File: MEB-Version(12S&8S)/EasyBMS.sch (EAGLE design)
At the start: 168 parts, among them IC1 XL7046, IC2 LTC6811IG-1#PBF, IC3 ISO1042DWV, IC4 C98655, J1 TYPE-C-31-M-12, Q14 C8547, Q15 C8547, Q16 C8547, Q18 C8547, Q20 C8547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

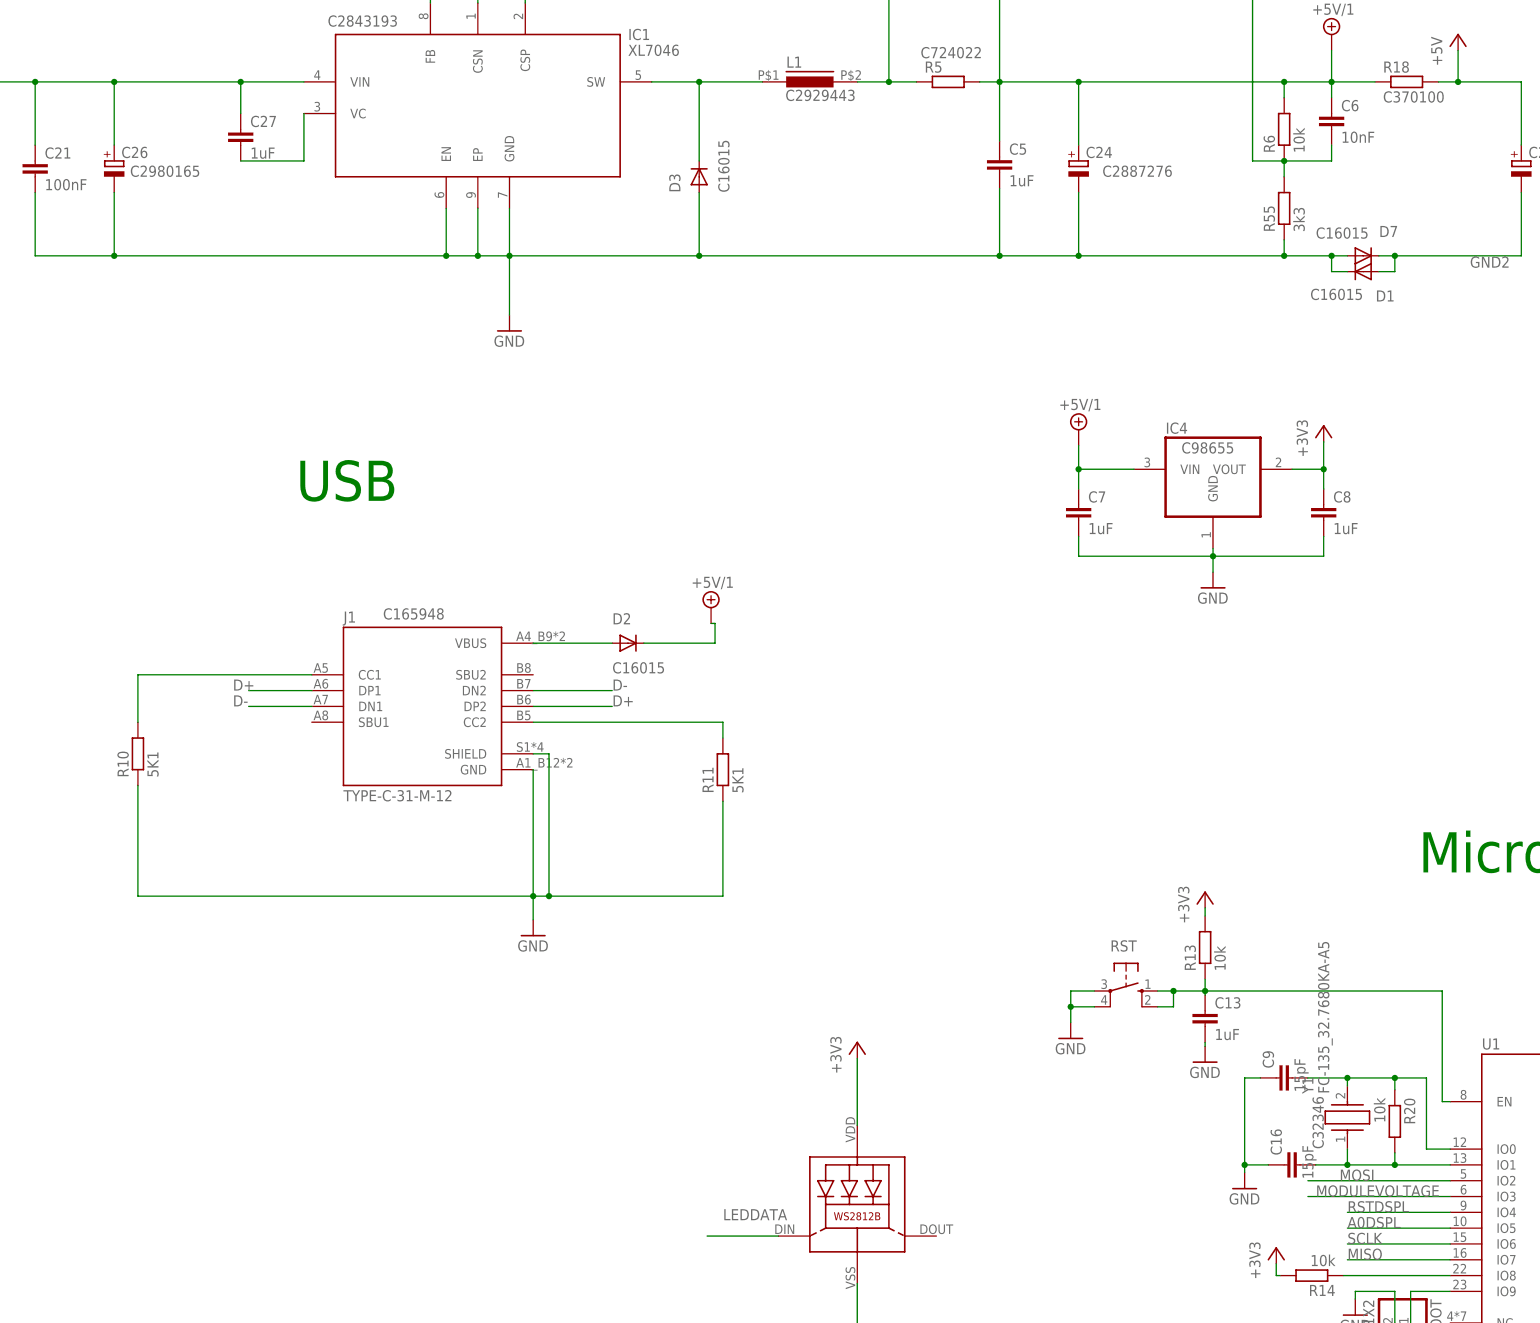
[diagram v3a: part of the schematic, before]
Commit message: change some parts to basic parts, add USB protection
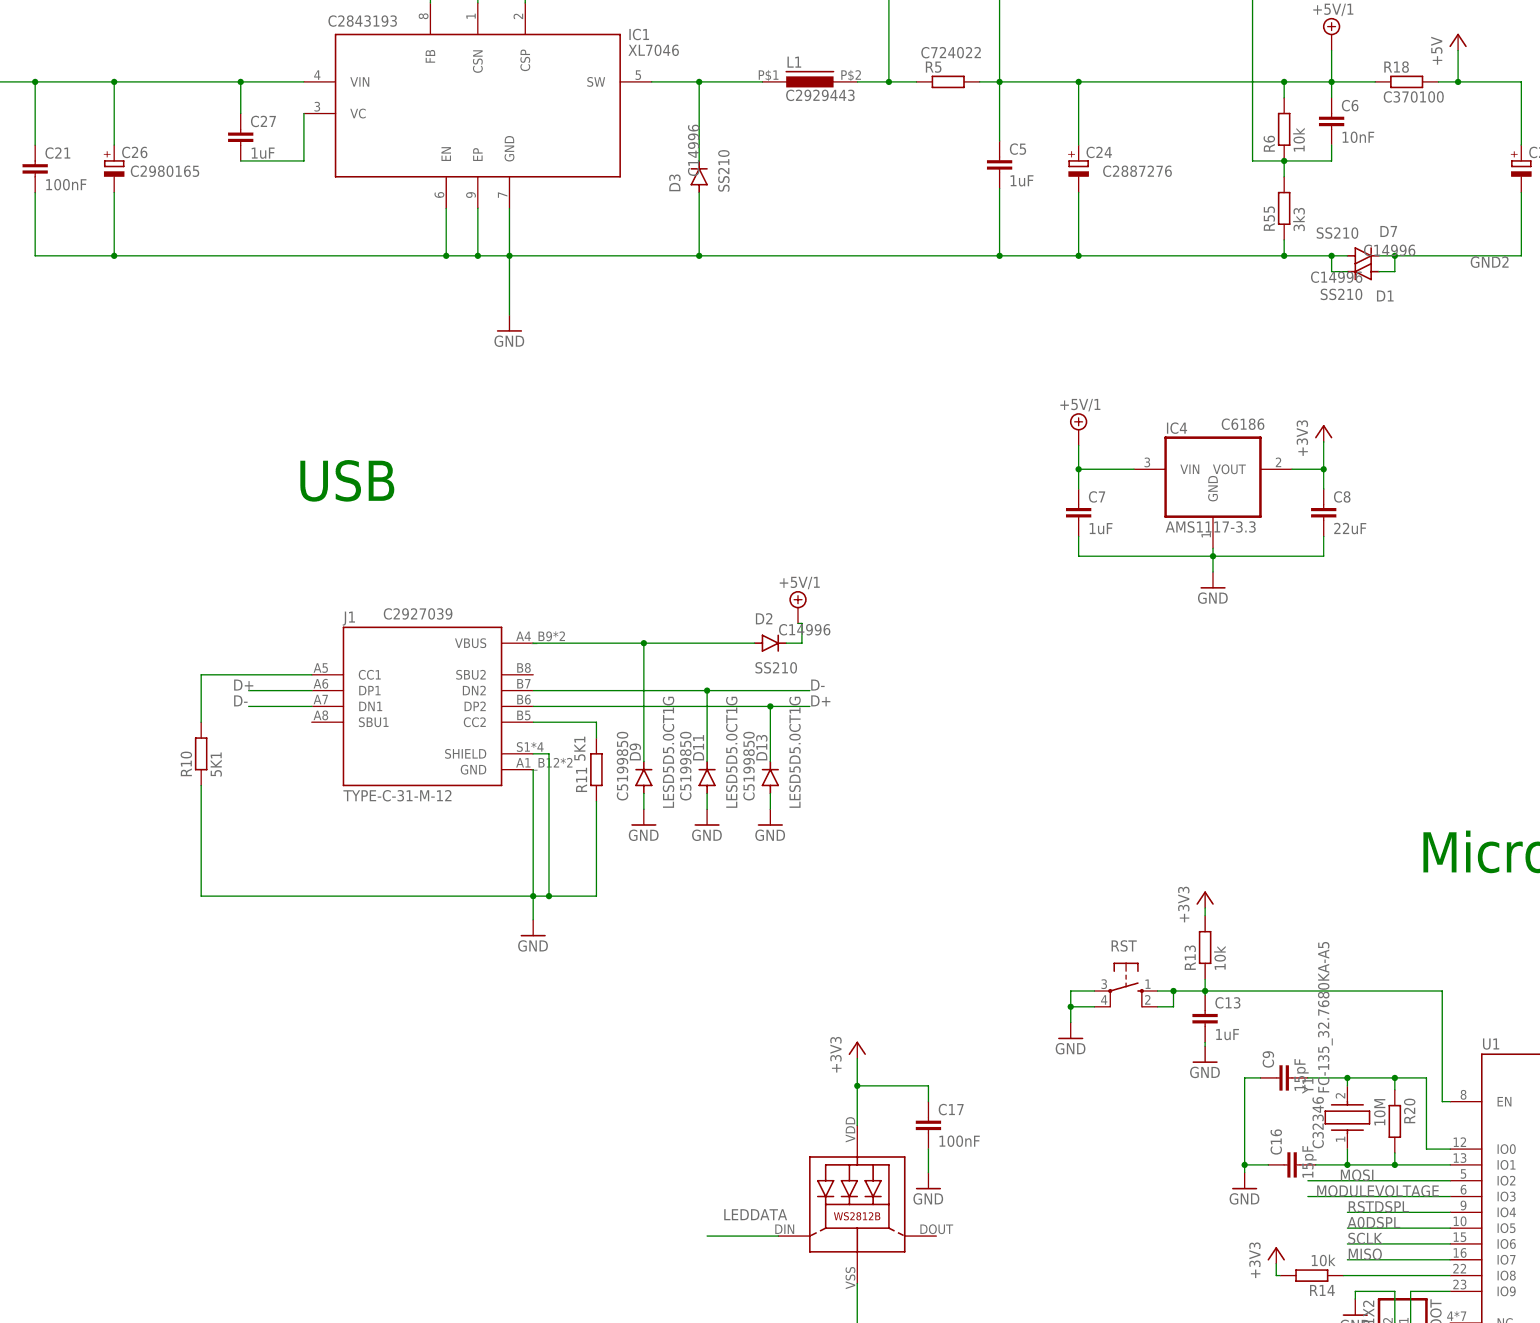
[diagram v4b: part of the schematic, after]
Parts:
- added C17: 100nF, rcl:C-EUC0402
- added D11, D13, D9: LESD5D5.0CT1G, diode:DIODE-SOD523
- C14: device rcl:C-EUC1206 -> rcl:C-EUC0805
- C8: value 1uF -> 22uF; device rcl:C-EUC0402 -> rcl:C-EUC0603
- D1, D2, D3, D7: value C16015 -> SS210; LCSC (none) -> C14996
- IC4: value C98655 -> AMS1117-3.3; LCSC (none) -> C6186
- J1: LCSC C165948 -> C2927039
- R20: value 10k -> 10M
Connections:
- net +3V3: now also C17.1
- net D+: now also D13.C
- net D-: now also D11.C
- net GND: now also C17.2, D11.A, D13.A, D9.A
- net N$4: now also D9.C
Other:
- moved on the sheet: R10, R11

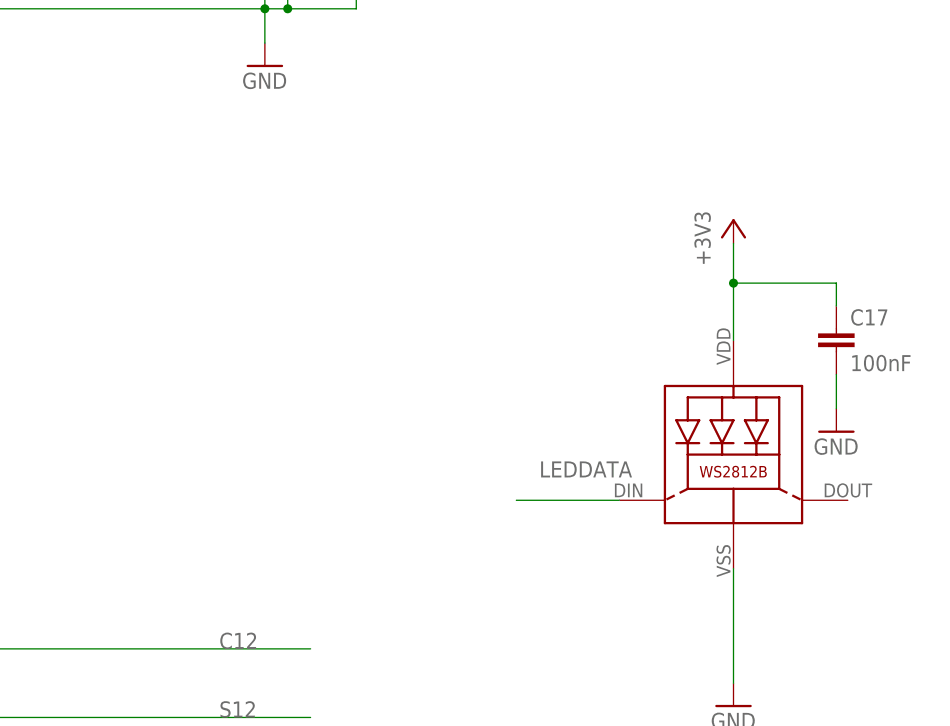
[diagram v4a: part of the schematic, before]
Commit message: change LED pixel circuit as in C6 Devkit
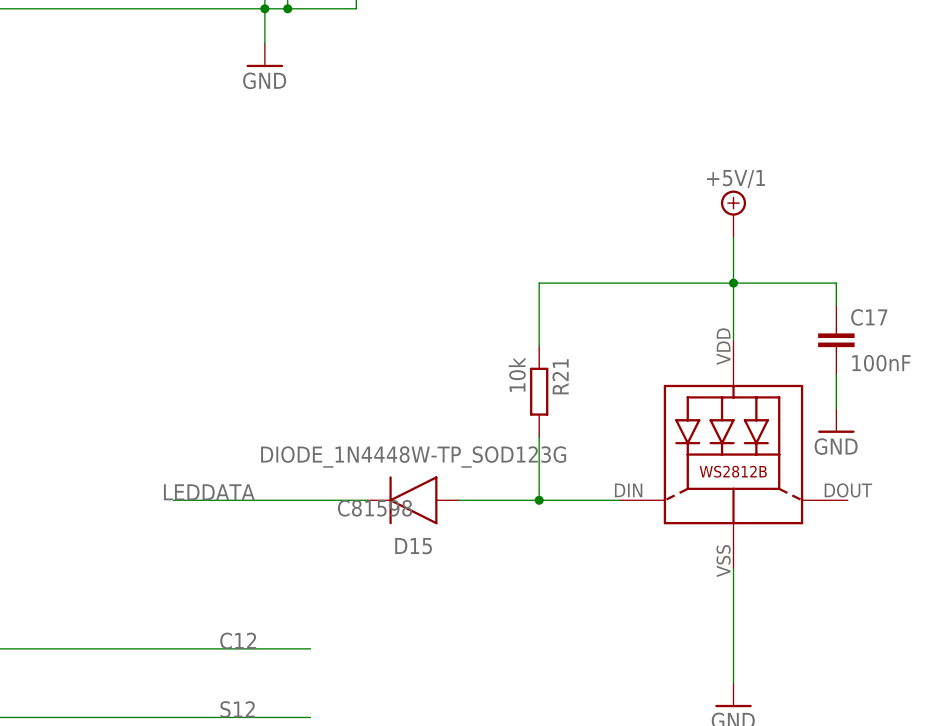
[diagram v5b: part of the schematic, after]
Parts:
- added D15: DIODE_1N4448W-TP_SOD123G, Diode:DIODE_1N4448W-TP_SOD123G
- added R21: 10k, rcl:R-EU_R0402
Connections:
- new net N$24: D15.A, LED2.DI, R21.2
- net +3V3: no longer C17.1, LED2.VDD
- net +5V/1: now also C17.1, LED2.VDD, R21.1
- net LEDDATA: now also D15.C; no longer LED2.DI
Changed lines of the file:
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@@
 <part name="TERM" library="jumper" library_urn="urn:adsk.eagle:library:252" deviceset="SJ" device="" package3d_urn="urn:adsk.eagle:package:15471/1"/>
 <part name="C12" library="rcl" library_urn="urn:adsk.eagle:library:334" deviceset="C-EU" device="C1206" package3d_urn="urn:adsk.eagle:package:23618/2" value="47µF"/>
-<part name="+3V7" library="supply1" library_urn="urn:adsk.eagle:library:371" deviceset="+3V3" device=""/>
 <part name="R13" library="rcl" library_urn="urn:adsk.eagle:library:334" deviceset="R-EU_" device="R0402" package3d_urn="urn:adsk.eagle:package:23547/3" value="10k"/>
 <part name="C13" library="rcl" library_urn="urn:adsk.eagle:library:334" deviceset="C-EU" device="C0402" package3d_urn="urn:adsk.eagle:package:23626/2" value="1uF"/>
@@
 <part name="GND18" library="supply1" library_urn="urn:adsk.eagle:library:371" deviceset="GND" device=""/>
 <part name="GND19" library="supply1" library_urn="urn:adsk.eagle:library:371" deviceset="GND" device=""/>
+<part name="SUPPLY3" library="supply2" library_urn="urn:adsk.eagle:library:372" deviceset="+5V/1" device=""/>
+<part name="D15" library="Diode" library_urn="urn:adsk.eagle:library:16378169" deviceset="DIODE_" device="_SOD123G" package3d_urn="urn:adsk.eagle:package:9427058/2" technology="1N4448W-TP">
+<attribute name="LCSC" value="C81598"/>
+</part>
+<part name="R21" library="rcl" library_urn="urn:adsk.eagle:library:334" deviceset="R-EU_" device="R0402" package3d_urn="urn:adsk.eagle:package:23547/3" value="10k"/>
 </parts>
 <sheets>
@@
 <attribute name="VALUE" x="-9.906" y="446.151" size="1.778" layer="96"/>
 </instance>
-<instance part="+3V7" gate="G$1" x="-220.98" y="511.175" smashed="yes">
-<attribute name="VALUE" x="-223.52" y="506.095" size="1.778" layer="96" rot="R90"/>
-</instance>
 <instance part="R13" gate="G$1" x="-165.1" y="526.415" smashed="yes" rot="R90">
 <attribute name="NAME" x="-166.5986" y="522.605" size="1.778" layer="95" rot="R90"/>
@@
 <attribute name="VALUE" x="-237.49" y="543.56" size="1.778" layer="96"/>
 </instance>
+<instance part="SUPPLY3" gate="G$1" x="-220.98" y="511.81" smashed="yes">
+<attribute name="VALUE" x="-224.155" y="514.985" size="1.778" layer="96"/>
+</instance>
+<instance part="D15" gate="G$1" x="-256.54" y="480.06" smashed="yes" rot="R180">
+<attribute name="NAME" x="-256.54" y="474.98" size="1.778" layer="95" rot="R180" align="center"/>
+<attribute name="VALUE" x="-256.54" y="485.14" size="1.778" layer="96" rot="R180" align="center"/>
+<attribute name="LCSC" x="-256.54" y="480.06" size="1.778" layer="96" rot="R180"/>
+</instance>
+<instance part="R21" gate="G$1" x="-242.57" y="492.125" smashed="yes" rot="R270">
+<attribute name="NAME" x="-241.0714" y="495.935" size="1.778" layer="95" rot="R270"/>
+<attribute name="VALUE" x="-245.872" y="495.935" size="1.778" layer="96" rot="R270"/>
+</instance>
 </instances>
 <busses>
@@
 </segment>
 <segment>
-<pinref part="LED2" gate="G$1" pin="VDD"/>
-<wire x1="-220.98" y1="497.84" x2="-220.98" y2="504.19" width="0.1524" layer="91"/>
-<pinref part="+3V7" gate="G$1" pin="+3V3"/>
-<pinref part="C17" gate="G$1" pin="1"/>
-<wire x1="-220.98" y1="504.19" x2="-220.98" y2="508.635" width="0.1524" layer="91"/>
-<wire x1="-220.98" y1="504.19" x2="-209.55" y2="504.19" width="0.1524" layer="91"/>
-<wire x1="-209.55" y1="504.19" x2="-209.55" y2="501.65" width="0.1524" layer="91"/>
-<junction x="-220.98" y="504.19"/>
-</segment>
-<segment>
 <pinref part="+3V5" gate="G$1" pin="+3V3"/>
 <pinref part="R13" gate="G$1" pin="2"/>
@@
 <wire x1="-53.34" y1="480.06" x2="-53.34" y2="490.22" width="0.1524" layer="91"/>
 </segment>
+<segment>
+<pinref part="LED2" gate="G$1" pin="VDD"/>
+<wire x1="-220.98" y1="497.84" x2="-220.98" y2="504.19" width="0.1524" layer="91"/>
+<pinref part="C17" gate="G$1" pin="1"/>
+<wire x1="-220.98" y1="504.19" x2="-220.98" y2="509.27" width="0.1524" layer="91"/>
+<wire x1="-220.98" y1="504.19" x2="-209.55" y2="504.19" width="0.1524" layer="91"/>
+<wire x1="-209.55" y1="504.19" x2="-209.55" y2="501.65" width="0.1524" layer="91"/>
+<junction x="-220.98" y="504.19"/>
+<pinref part="SUPPLY3" gate="G$1" pin="+5V/1"/>
+<pinref part="R21" gate="G$1" pin="1"/>
+<wire x1="-242.57" y1="497.205" x2="-242.57" y2="504.19" width="0.1524" layer="91"/>
+<wire x1="-242.57" y1="504.19" x2="-220.98" y2="504.19" width="0.1524" layer="91"/>
+</segment>
 </net>
 <net name="C12+POWER" class="0">
@@
 <net name="LEDDATA" class="0">
 <segment>
-<pinref part="LED2" gate="G$1" pin="DI"/>
-<wire x1="-233.68" y1="480.06" x2="-245.11" y2="480.06" width="0.1524" layer="91"/>
-<label x="-242.57" y="482.6" size="1.778" layer="95"/>
-</segment>
-<segment>
 <pinref part="U1" gate="G$1" pin="IO14"/>
 <wire x1="-95.25" y1="488.95" x2="-85.09" y2="488.95" width="0.1524" layer="91"/>
 <label x="-95.25" y="488.95" size="1.778" layer="95"/>
 </segment>
+<segment>
+<pinref part="D15" gate="G$1" pin="C"/>
+<wire x1="-261.62" y1="480.06" x2="-283.21" y2="480.06" width="0.1524" layer="91"/>
+<label x="-284.48" y="480.06" size="1.778" layer="95"/>
+</segment>
 </net>
 <net name="SCLK" class="0">
@@
 </segment>
 </net>
+<net name="N$24" class="0">
+<segment>
+<pinref part="LED2" gate="G$1" pin="DI"/>
+<pinref part="D15" gate="G$1" pin="A"/>
+<wire x1="-233.68" y1="480.06" x2="-242.57" y2="480.06" width="0.1524" layer="91"/>
+<pinref part="R21" gate="G$1" pin="2"/>
+<wire x1="-242.57" y1="480.06" x2="-251.46" y2="480.06" width="0.1524" layer="91"/>
+<wire x1="-242.57" y1="487.045" x2="-242.57" y2="480.06" width="0.1524" layer="91"/>
+<junction x="-242.57" y="480.06"/>
+</segment>
+</net>

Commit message: new Footprint to change to basic parts
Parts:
- C12, C14: value 47µF -> 47uF
- R15, R16: device rcl:R-EU_R0402 -> rcl:R-EU_R0603
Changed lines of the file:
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@@
 </classes>
 <parts>
-<part name="R15" library="rcl" library_urn="urn:adsk.eagle:library:334" deviceset="R-EU_" device="R0402" package3d_urn="urn:adsk.eagle:package:23547/3" value="470k"/>
-<part name="R16" library="rcl" library_urn="urn:adsk.eagle:library:334" deviceset="R-EU_" device="R0402" package3d_urn="urn:adsk.eagle:package:23547/3" value="27K"/>
+<part name="R15" library="rcl" library_urn="urn:adsk.eagle:library:334" deviceset="R-EU_" device="R0603" package3d_urn="urn:adsk.eagle:package:23555/3" value="470k"/>
+<part name="R16" library="rcl" library_urn="urn:adsk.eagle:library:334" deviceset="R-EU_" device="R0603" package3d_urn="urn:adsk.eagle:package:23555/3" value="27K"/>
 <part name="C4" library="rcl" library_urn="urn:adsk.eagle:library:334" deviceset="C-EU" device="C0402" package3d_urn="urn:adsk.eagle:package:23626/2" value="1uF"/>
 <part name="C19" library="rcl" library_urn="urn:adsk.eagle:library:334" deviceset="C-EU" device="C0402" package3d_urn="urn:adsk.eagle:package:23626/2" value="1uF"/>
@@
 <part name="R12" library="rcl" library_urn="urn:adsk.eagle:library:334" deviceset="R-EU_" device="R0402" package3d_urn="urn:adsk.eagle:package:23547/3" value="120R"/>
 <part name="TERM" library="jumper" library_urn="urn:adsk.eagle:library:252" deviceset="SJ" device="" package3d_urn="urn:adsk.eagle:package:15471/1"/>
-<part name="C12" library="rcl" library_urn="urn:adsk.eagle:library:334" deviceset="C-EU" device="C1206" package3d_urn="urn:adsk.eagle:package:23618/2" value="47µF"/>
+<part name="C12" library="rcl" library_urn="urn:adsk.eagle:library:334" deviceset="C-EU" device="C1206" package3d_urn="urn:adsk.eagle:package:23618/2" value="47uF"/>
 <part name="R13" library="rcl" library_urn="urn:adsk.eagle:library:334" deviceset="R-EU_" device="R0402" package3d_urn="urn:adsk.eagle:package:23547/3" value="10k"/>
 <part name="C13" library="rcl" library_urn="urn:adsk.eagle:library:334" deviceset="C-EU" device="C0402" package3d_urn="urn:adsk.eagle:package:23626/2" value="1uF"/>
 <part name="GND11" library="supply1" library_urn="urn:adsk.eagle:library:371" deviceset="GND" device=""/>
-<part name="C14" library="rcl" library_urn="urn:adsk.eagle:library:334" deviceset="C-EU" device="C0805" package3d_urn="urn:adsk.eagle:package:23617/2" value="47µF"/>
+<part name="C14" library="rcl" library_urn="urn:adsk.eagle:library:334" deviceset="C-EU" device="C0805" package3d_urn="urn:adsk.eagle:package:23617/2" value="47uF"/>
 <part name="GND12" library="supply1" library_urn="urn:adsk.eagle:library:371" deviceset="GND" device=""/>
 <part name="C15" library="rcl" library_urn="urn:adsk.eagle:library:334" deviceset="C-EU" device="C0402" package3d_urn="urn:adsk.eagle:package:23626/2" value="100nF"/>
